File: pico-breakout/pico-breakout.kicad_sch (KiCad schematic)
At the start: 6 parts, among them J1 Conn_01x20, J2 Conn_01x20, J3 Conn_01x20, J4 Conn_01x20, J5 Conn_01x03, J6 Conn_01x03

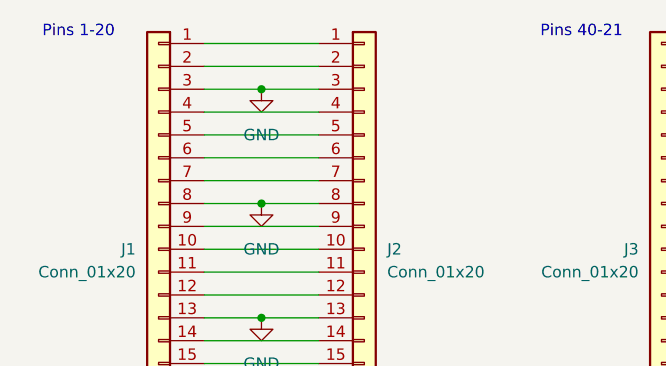
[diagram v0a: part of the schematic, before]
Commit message: Add series resistor to GPIO 2
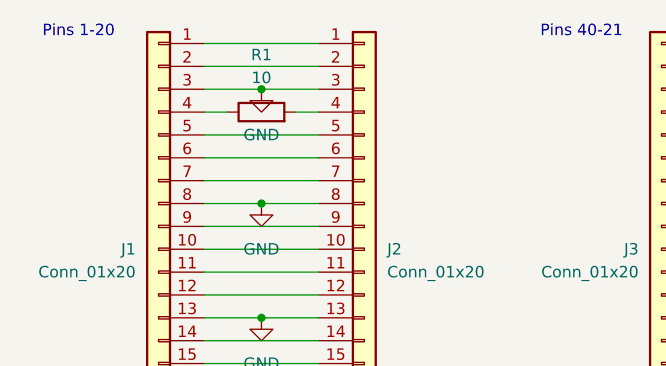
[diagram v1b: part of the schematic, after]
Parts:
- added R1: 10, Resistor_SMD:R_0603_1608Metric, symbol Device:R
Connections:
- net at J1.4 (Pin_4): now also R1.1; no longer J2.4 (Pin_4)
- new net: J2.4 (Pin_4), R1.2
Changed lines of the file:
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@@
-	(wire
-		(pts
-			(xy 35.56 27.94) (xy 48.26 27.94)
-		)
-		(stroke
-			(width 0)
-			(type default)
-		)
-	)
 	(wire
 		(pts
@@
 	(wire
 		(pts
+			(xy 35.56 27.94) (xy 38.1 27.94)
+		)
+		(stroke
+			(width 0)
+			(type default)
+		)
+	)
+	(wire
+		(pts
 			(xy 35.56 20.32) (xy 48.26 20.32)
 		)
@@
 		(pts
 			(xy 35.56 33.02) (xy 48.26 33.02)
+		)
+		(stroke
+			(width 0)
+			(type default)
+		)
+	)
+	(wire
+		(pts
+			(xy 45.72 27.94) (xy 48.26 27.94)
 		)
 		(stroke
@@
 			)
 		)
+	)
+	(symbol
+		(lib_id "Device:R")
+		(at 41.91 27.94 90)
+		(unit 1)
+		(exclude_from_sim no)
+		(in_bom yes)
+		(on_board yes)
+		(dnp no)
+		(fields_autoplaced yes)
+		(property "Reference" "R1"
+			(at 41.91 21.59 90)
+			(effects
+				(font
+					(size 1.27 1.27)
+				)
+			)
+		)
+		(property "Value" "10"
+			(at 41.91 24.13 90)
+			(effects
+				(font
+					(size 1.27 1.27)
+				)
+			)
+		)
+		(property "Footprint" "Resistor_SMD:R_0603_1608Metric"
+			(at 41.91 29.718 90)
+			(effects
+				(font
+					(size 1.27 1.27)
+				)
+				(hide yes)
+			)
+		)
+		(property "Datasheet" "~"
+			(at 41.91 27.94 0)
+			(effects
+				(font
+					(size 1.27 1.27)
+				)
+				(hide yes)
+			)
+		)
+		(property "Description" "Resistor"
+			(at 41.91 27.94 0)
+			(effects
+				(font
+					(size 1.27 1.27)
+				)
+				(hide yes)
+			)
+		)
+		(pin "1"
+		)
+		(pin "2"
+		)
+		(instances
+			(project ""
+				(path "/18c791f4-e940-4e36-b51d-61b81c54794f"
+					(reference "R1")
+					(unit 1)
+				)
+			)
+		)
